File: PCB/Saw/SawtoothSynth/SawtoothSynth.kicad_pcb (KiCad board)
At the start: 4 copper layers, 203.2 x 203.2 mm, 38 parts, among them Q1 SS8550, U1 NE555D, U2 LM358, U3 LM386, U5 4017, U7 LD1117S50TR_SOT223

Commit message: Routed LED in Circle
Routed LED's in circle around PCB.
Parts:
- moved D9 653.8 mm to (-326.4, -254.5), turned to -91.635 degrees
- moved D8 648.9 mm to (-326.4, -194.8), turned to 124.365 degrees
- moved U5 647.5 mm to (-325.0, -223.2)
- moved D10 627.9 mm to (-291.3, -302.8), turned to -127.635 degrees
- moved D7 614.3 mm to (-291.3, -146.5), turned to -19.635 degrees
- moved R8 588.9 mm to (-258.5, -317.2), turned to 180 degrees
- moved D11 578.0 mm to (-234.5, -321.3), turned to -163.635 degrees
- moved D6 553.2 mm to (-234.5, -128.1), turned to 16.365 degrees
- moved D2 510.6 mm to (-177.7, -302.8), turned to 160.365 degrees
- moved D5 495.7 mm to (-177.7, -146.5), turned to 52.365 degrees
- moved D3 466.9 mm to (-142.6, -254.5), turned to 124.365 degrees
- moved D4 460.6 mm to (-142.6, -194.8), turned to 88.365 degrees
- moved D1 249.6 mm to (192.4, 17.0), turned to 163.635 degrees
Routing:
- net Net-(D10-K): track 0.00 -> 590.3 mm
- net Net-(D4-A): track 0.00 -> 316.8 mm, vias 0 -> 2
- net Net-(D3-A): track 0.00 -> 281.5 mm, vias 0 -> 2
- net Net-(D2-A): track 0.00 -> 273.0 mm, vias 0 -> 2
- net Net-(D5-A): track 0.00 -> 236.1 mm, vias 0 -> 2
- net Net-(D6-A): track 0.00 -> 160.8 mm, vias 0 -> 2
- net Net-(D11-A): track 0.00 -> 152.0 mm, vias 0 -> 2
- net Net-(D7-A): track 0.00 -> 106.8 mm, vias 0 -> 2
- net Net-(D10-A): track 0.00 -> 99.8 mm, vias 0 -> 2
- net Net-(D9-A): track 0.00 -> 39.7 mm, vias 0 -> 2
- net Net-(D8-A): track 0.00 -> 31.8 mm
- added copper zone on In2.Cu, net +12V
- added copper zone on In1.Cu, net GND
- removed copper zone on In1.Cu, net (none)
- removed copper zone on In2.Cu, net (none)

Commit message: Laid Out PCB  No DRC Errors
Finished laying out PCB, no DRC errors
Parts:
- moved Q1 578.5 mm to (-246.2, -186.3), turned to -90 degrees
- moved U1 577.2 mm to (-257.2, -178.2)
- moved U2 577.2 mm to (-248.2, -168.5)
- moved RV2 565.8 mm to (-238.2, -167.0)
- moved R4 563.9 mm to (-255.5, -164.2), turned to -90 degrees
- moved R3 563.9 mm to (-255.5, -169.6), turned to 90 degrees
- moved C2 563.8 mm to (-251.0, -175.5), turned to -90 degrees
- moved RV1 562.9 mm to (-235.8, -181.5), turned to 90 degrees
- moved C1 559.0 mm to (-246.2, -175.5), turned to -90 degrees
- moved U3 557.4 mm to (-228.5, -167.7)
- moved RoundDispTFT1 555.6 mm to (-235.9, -239.3)
- moved R2 554.6 mm to (-246.2, -180.2), turned to -90 degrees
- moved C4 554.3 mm to (-241.5, -175.5), turned to 90 degrees
- moved R1 548.4 mm to (-240.0, -183.0)
- moved R5 546.2 mm to (-237.8, -175.5), turned to -90 degrees
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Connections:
- Q1 pad 1: unconnected-(Q1-B-Pad1) -> Net-(D1-K)
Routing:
- net SAWTOOTH_555: track 0.00 -> 108.5 mm
- net GND: track 0.00 -> 88.1 mm, vias 0 -> 12
- net SAWTOOTH_MICRO: track 0.00 -> 65.5 mm
- net +5V: track 0.00 -> 63.6 mm
- net DAC: track 0.00 -> 48.8 mm, vias 0 -> 2
- net SPI_MOSI: track 0.00 -> 30.1 mm
- net SPI_DC: track 0.00 -> 23.3 mm
- net SPI_CS: track 0.00 -> 22.8 mm
- net +12V: track 0.00 -> 20.5 mm, vias 0 -> 8
- net SPI_SCK: track 0.00 -> 19.8 mm, vias 0 -> 2
- net Net-(C6-Pad2): track 0.00 -> 14.6 mm
- net SPI_RST: track 0.00 -> 14.3 mm
- net Net-(BATT1-+): track 0.00 -> 12.1 mm
- net Net-(U2B--): track 0.00 -> 11.4 mm
- net Net-(U7-VO): track 0.00 -> 10.4 mm
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
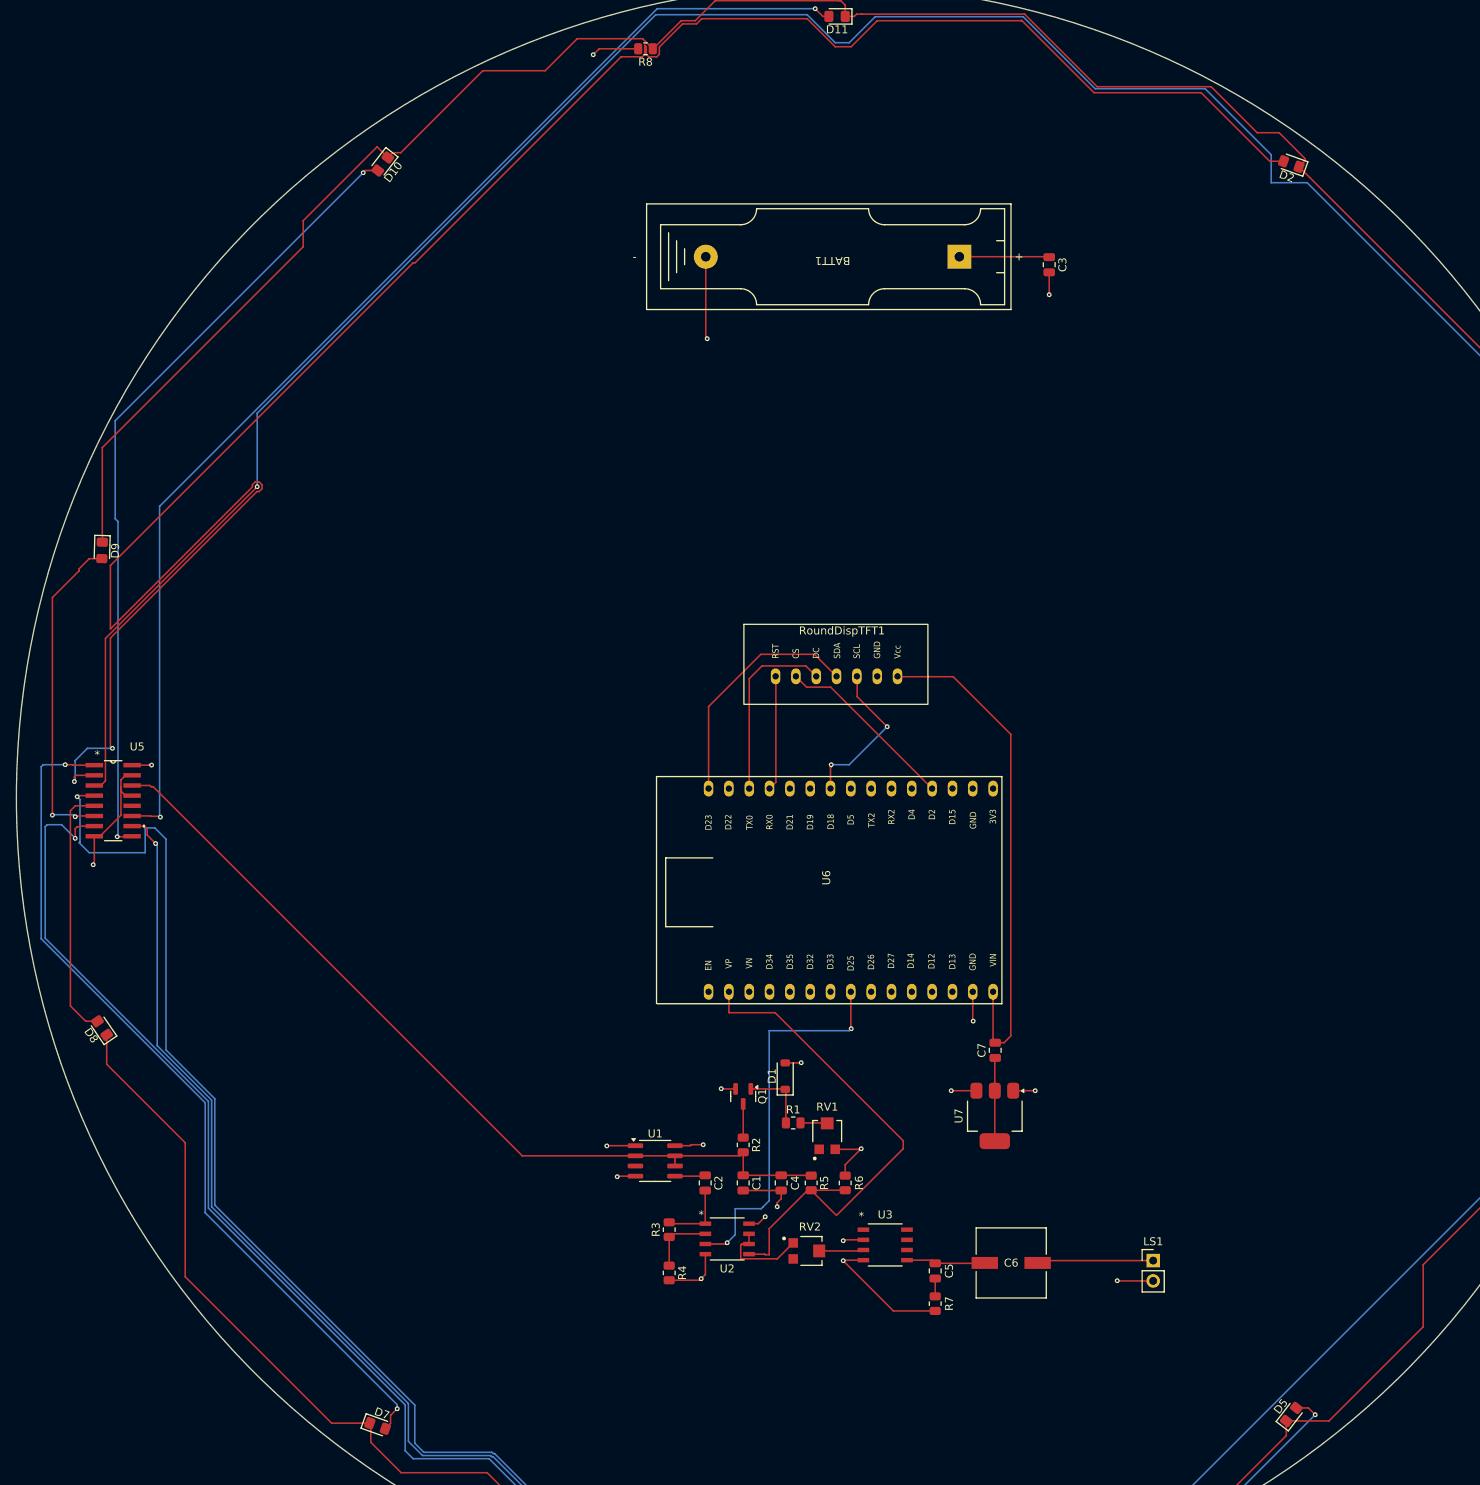
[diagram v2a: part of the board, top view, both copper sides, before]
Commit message: Added Mounting Holes/Touch, Changed to 2-Layer Board
Added 3 standard M4 mounting holes for standoff and 1 M4 mounting hole connected to touch pin on micro.

I changed the board to a 2 layer since adding a solid copper pour for GND or PWR would ruin the transparent aesthetic
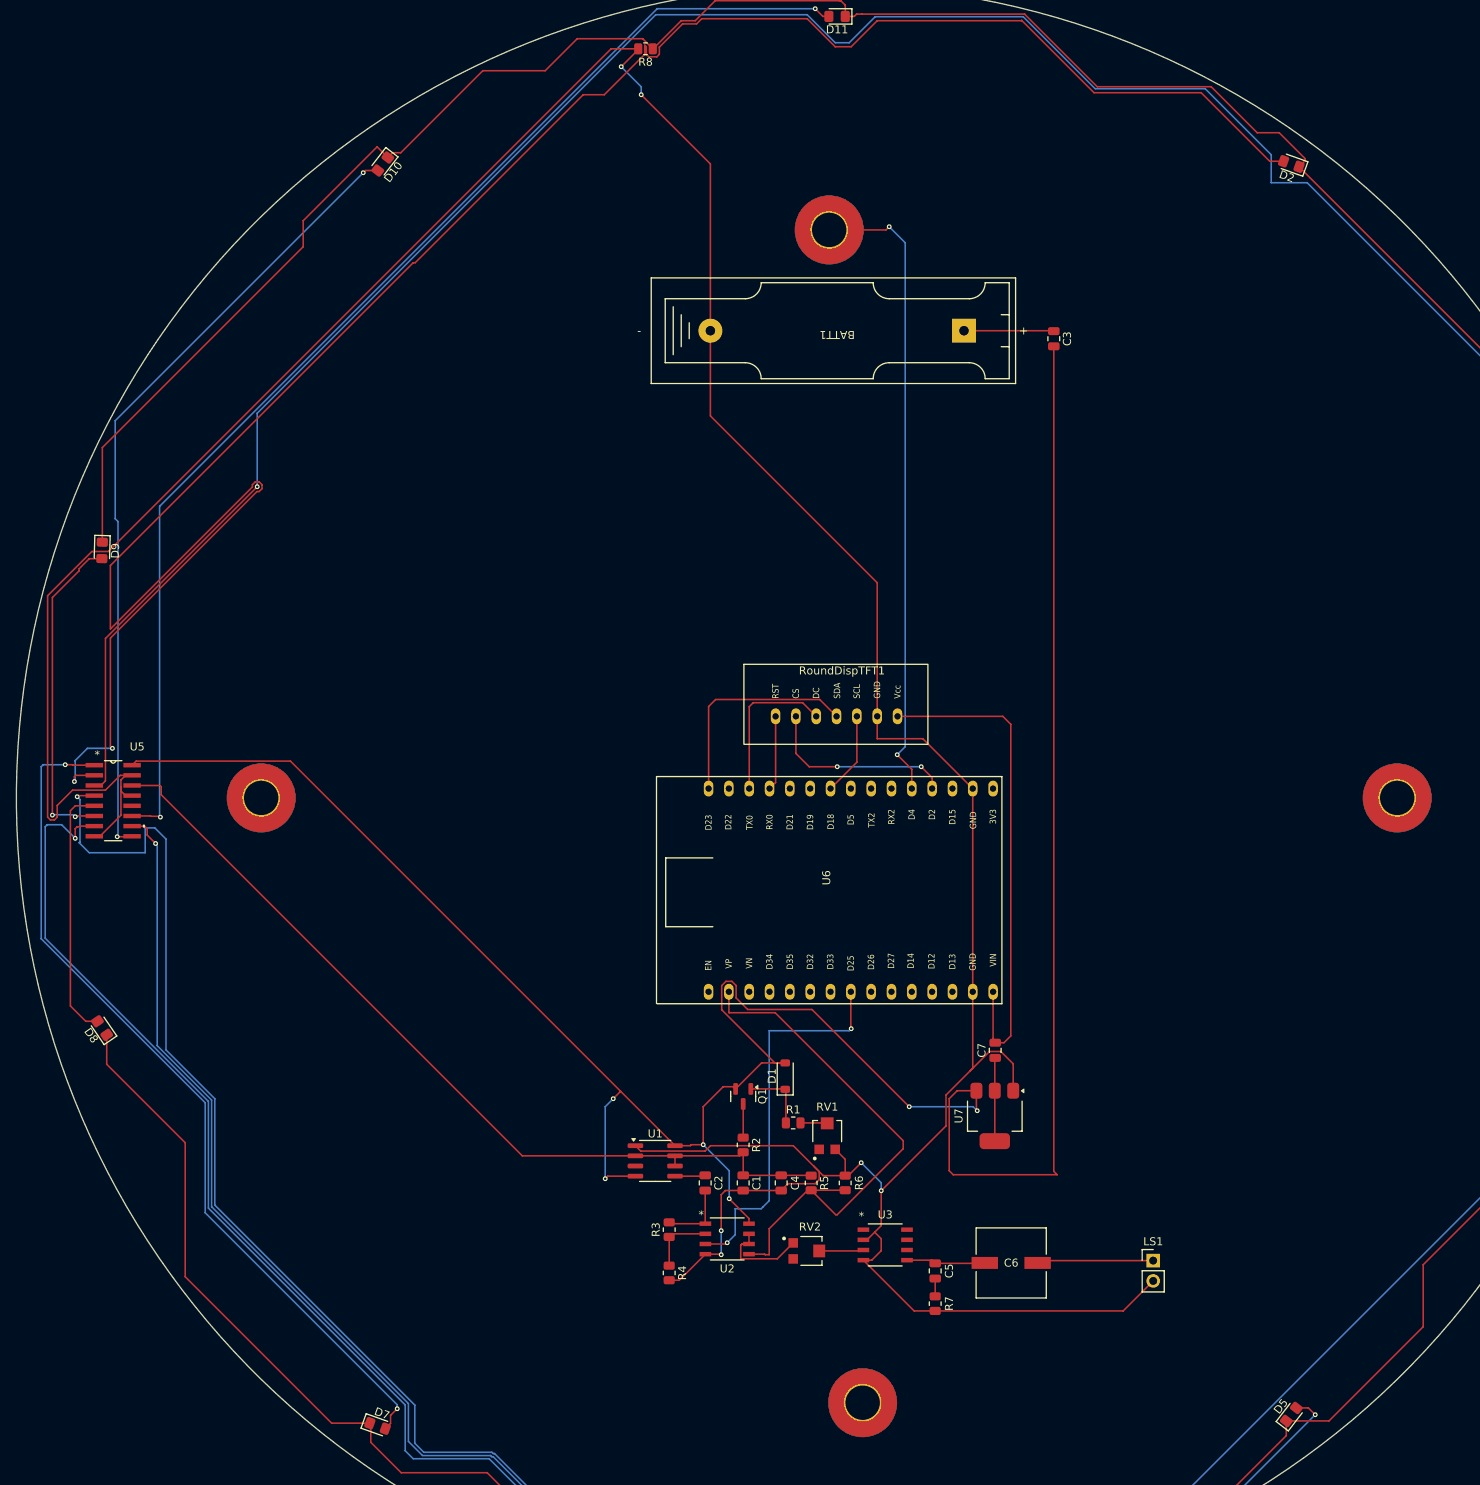
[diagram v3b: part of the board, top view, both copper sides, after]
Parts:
- added MOUNTING1: MountingHole_Pad, MountingHole:MountingHole_4.3mm_M4_Pad_TopBottom, F.Cu at (-231.3, -148.0)
- added MOUNTING2: MountingHole_Pad, MountingHole:MountingHole_4.3mm_M4_Pad_TopBottom, F.Cu at (-306.5, -223.6)
- added MOUNTING3: MountingHole_Pad, MountingHole:MountingHole_4.3mm_M4_Pad_TopBottom, F.Cu at (-164.5, -223.6)
- added TOUCH1: MountingHole_Pad, MountingHole:MountingHole_4.3mm_M4_Pad_TopBottom, F.Cu at (-235.5, -294.6)
- moved BATT1 9.27 mm to (-234.5, -282.0)
- moved C3 9.27 mm to (-207.4, -281.0)
- moved RoundDispTFT1 5.00 mm to (-235.9, -234.3)
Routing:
- net GND: track 88.1 -> 459.5 mm, vias 12 -> 6
- net +12V: track 20.5 -> 323.2 mm, vias 8 -> 6
- net TOUCH: track 0.00 -> 79.9 mm, vias 0 -> 2
- net SPI_SCK: track 19.8 -> 10.4 mm, vias 2 -> 0
- net SPI_RST: track 14.3 -> 9.34 mm
- net SPI_DC: track 23.3 -> 19.5 mm
- net SPI_MOSI: track 30.1 -> 27.5 mm
- net SPI_CS: track 22.8 -> 24.3 mm, vias 0 -> 2
- net +5V: track 63.6 -> 62.3 mm
- net SAWTOOTH_555: track 108.5 -> 109.0 mm
- removed copper zone on In2.Cu, net +12V
- removed copper zone on In1.Cu, net GND
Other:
- copper layers 4 -> 2

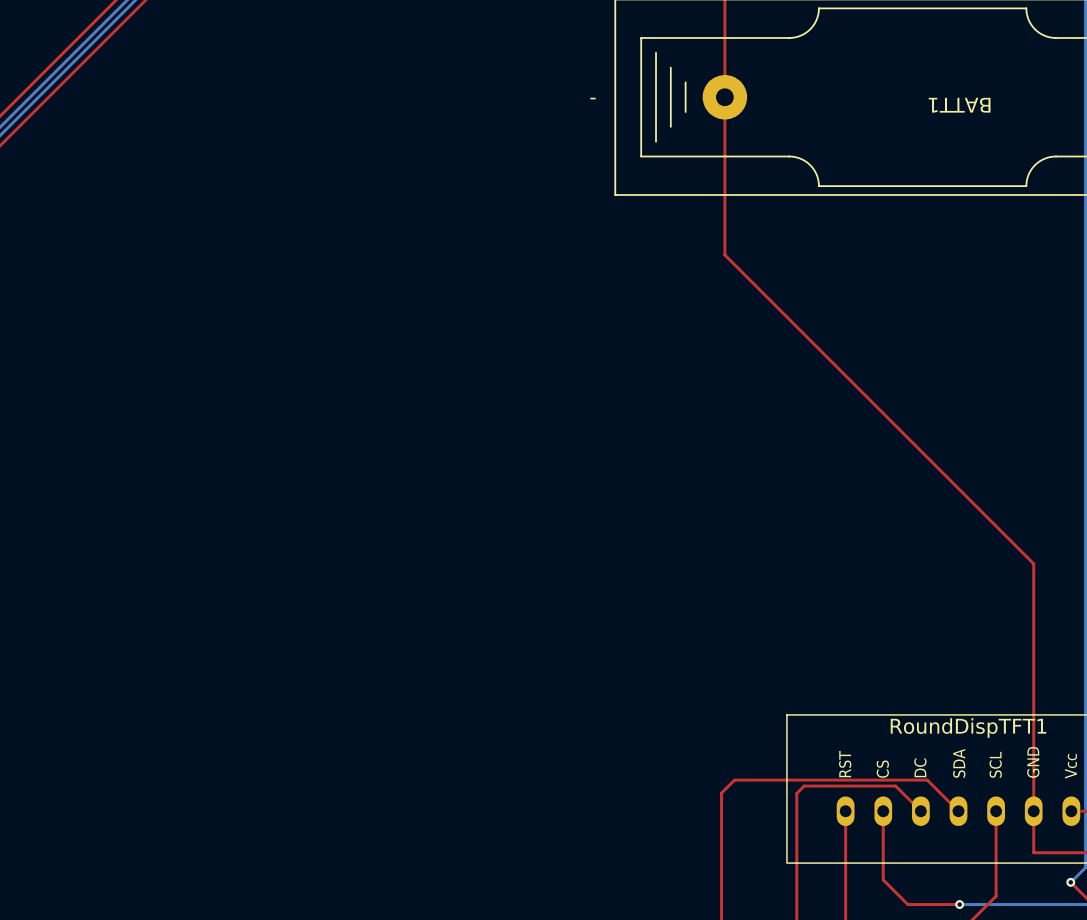
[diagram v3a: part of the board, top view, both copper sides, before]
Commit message: Updated Font, Added Silk Screen Graphic, Changed Board Stackup to Transparent
Updated Font, added silkscreen art of 555 sawtooth schematic, and signature

Modified board stackup colors and opacity to minimum in order to see transparent PCB
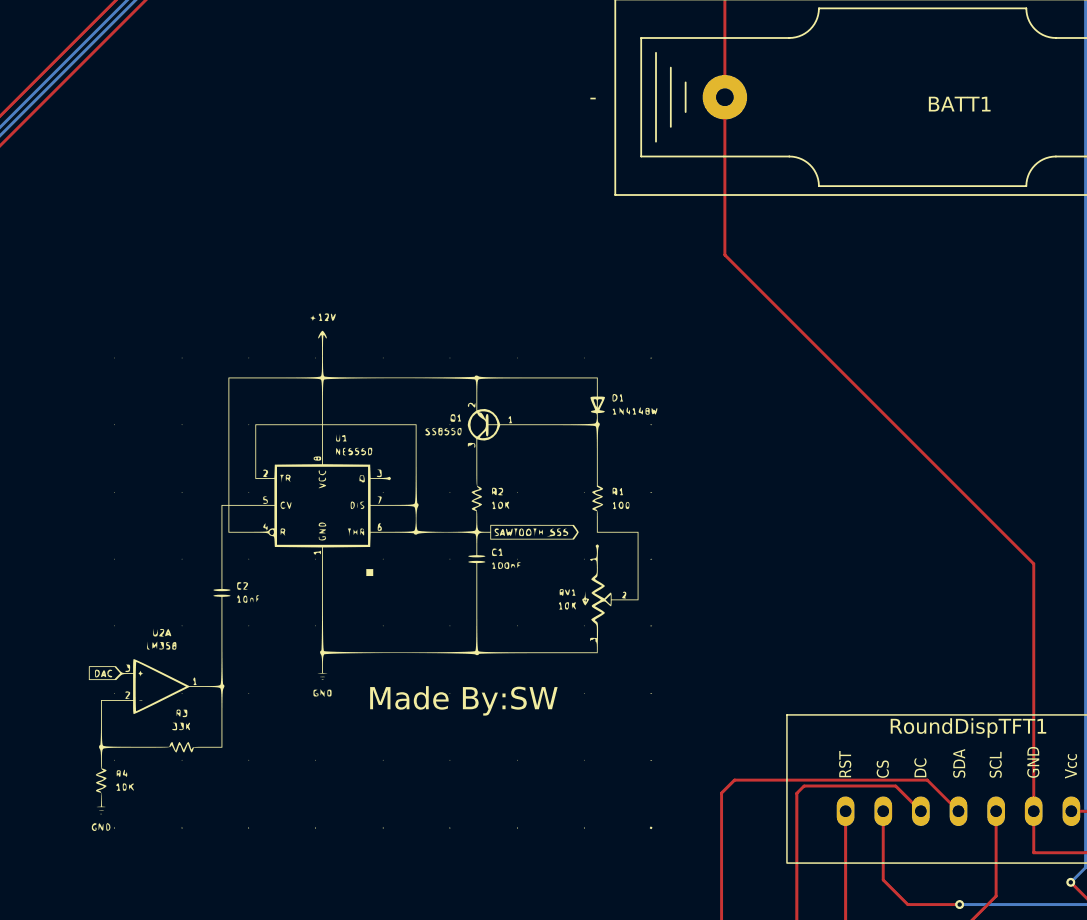
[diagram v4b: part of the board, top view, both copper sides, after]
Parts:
- added G***: LOGO, Custom SIlkscreens:555 Saw Diagram, F.Cu at (-274.5, -250.0)
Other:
- board text added: "Made By:SW"

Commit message: Added SPST Switch & DRC Fixes
Added SPST Toggle Switch to Schematic and PCB, Fixed Font DRC Errors & Courtyard Error For Silkscreen.

No DRC Errors
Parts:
- added SW1: SW_SPST, CustomLibrary:SW_SPST_Toggle, F.Cu at (-204.3, -211.5)
- moved G*** 1.12 mm to (-273.5, -250.5)
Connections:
- C3 pad 2: +12V -> Net-(SW1-A)
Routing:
- net Net-(SW1-A): track 0.00 -> 72.6 mm
- net +12V: track 323.2 -> 256.1 mm

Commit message: Routed Step-Up Circuitry, Updated PCB Battery Footprint, Moved Speaker
Routed Step-Up Circuitry on PCB, Changed 23A battery to 18650 on PCB, moved speaker footprint to bottom of PCB
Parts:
- added C10: 100uF, CustomLibrary:865060445005, F.Cu at (-173.0, -245.5)
- added C11: 1nF, Capacitor_SMD:C_0805_2012Metric, F.Cu at (-185.0, -252.5)
- added C9: 100uF, CustomLibrary:865060445005, F.Cu at (-203.0, -252.0)
- added CR1: 2STN1360, Package_TO_SOT_SMD:SOT-223-3_TabPin2, F.Cu at (-192.5, -247.5)
- added D12: MBR340, Diode_SMD:D_SMA, F.Cu at (-192.5, -255.5)
- added L1: 100uH, CustomLibrary:IND_BOURNS_SRN8040, F.Cu at (-178.9, -265.0)
- added R10: 12K, Resistor_SMD:R_0805_2012Metric, F.Cu at (-185.4, -235.5)
- added R11: 1.5K, Resistor_SMD:R_0805_2012Metric, F.Cu at (-191.0, -235.9)
- added R12: 0.22, Resistor_SMD:R_0805_2012Metric, F.Cu at (-172.0, -252.5)
- added R9: 180, Resistor_SMD:R_0805_2012Metric, F.Cu at (-171.6, -256.0)
- added RV3: 1K, CustomLibrary:TRIM_TC33X-2-103E, F.Cu at (-178.0, -236.0)
- added U4: MC34063AD, Package_SO:SOIC-8_3.9x4.9mm_P1.27mm, F.Cu at (-179.0, -254.1)
- BATT1: footprint CustomLibrary:BH23APC -> CustomLibrary:18650PC Battery Holder 1043P
- moved C3 55.0 mm to (-195.0, -227.4)
- moved LS1 47.3 mm to (-230.5, -134.5), turned to -90 degrees
- moved TOUCH1 15.9 mm to (-235.5, -310.5)
- moved BATT1 10.0 mm to (-234.0, -292.0)
- moved G*** 9.62 mm to (-282.0, -246.0)
- moved RoundDispTFT1 0.80 mm to (-235.9, -233.5)
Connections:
- SW1 pad 2: +12V -> +3V3
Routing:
- net GND: track 459.5 -> 597.3 mm, vias 6 -> 8
- net Net-(BATT1-+): track 12.1 -> 135.2 mm
- net +12V: track 256.1 -> 326.0 mm, vias 6 -> 8
- net +3V3: track 0.00 -> 61.5 mm
- net Net-(SW1-A): track 72.6 -> 14.1 mm
- net Net-(D12-A): track 0.00 -> 33.1 mm
- net Net-(C6-Pad2): track 14.6 -> 42.2 mm
- net Net-(U4-Vfb): track 0.00 -> 25.5 mm, vias 0 -> 2
- net Net-(U4-Ipk): track 0.00 -> 22.9 mm
- net Net-(U4-SwE): track 0.00 -> 20.9 mm, vias 0 -> 2
- net TOUCH: track 79.9 -> 90.8 mm
- net Net-(R10-Pad2): track 0.00 -> 8.57 mm
- net Net-(U4-DC): track 0.00 -> 4.05 mm
- net Net-(U4-TC): track 0.00 -> 3.50 mm

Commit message: Moved buttom mounting hole to be centered
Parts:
- moved MOUNTING1 4.19 mm to (-235.5, -148.0)

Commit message: Removed 5V Regulator
Removed 5V Regulator due to PCB being powered by 3.3-3.7V battery. Using a 5V regulator would just be a waste of energy
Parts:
- removed C7: 10nF, Capacitor_SMD:C_0805_2012Metric
- removed U7: LD1117S50TR_SOT223, Package_TO_SOT_SMD:SOT-223-3_TabPin2
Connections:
- RoundDispTFT1 pad 1: +5V -> +3V3
- U6 pad 2: +5V -> +3V3
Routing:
- net +3V3: track 61.5 -> 151.4 mm, vias 0 -> 2
- net +5V: track 62.3 -> 0.00 mm
- net +12V: track 326.0 -> 292.0 mm
- net GND: track 597.3 -> 617.9 mm
- net Net-(U7-VO): track 10.4 -> 0.00 mm
- net SAWTOOTH_MICRO: track 65.5 -> 61.7 mm
- net DAC: track 48.8 -> 49.4 mm
